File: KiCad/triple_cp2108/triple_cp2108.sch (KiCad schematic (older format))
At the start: 29 parts, among them J1 USB_B, J2 USB_A, J3 Conn_02x20_Odd_Even, U1 MIC5504-3.3YM5, U2 USB2514B_Bi, Y1 24M

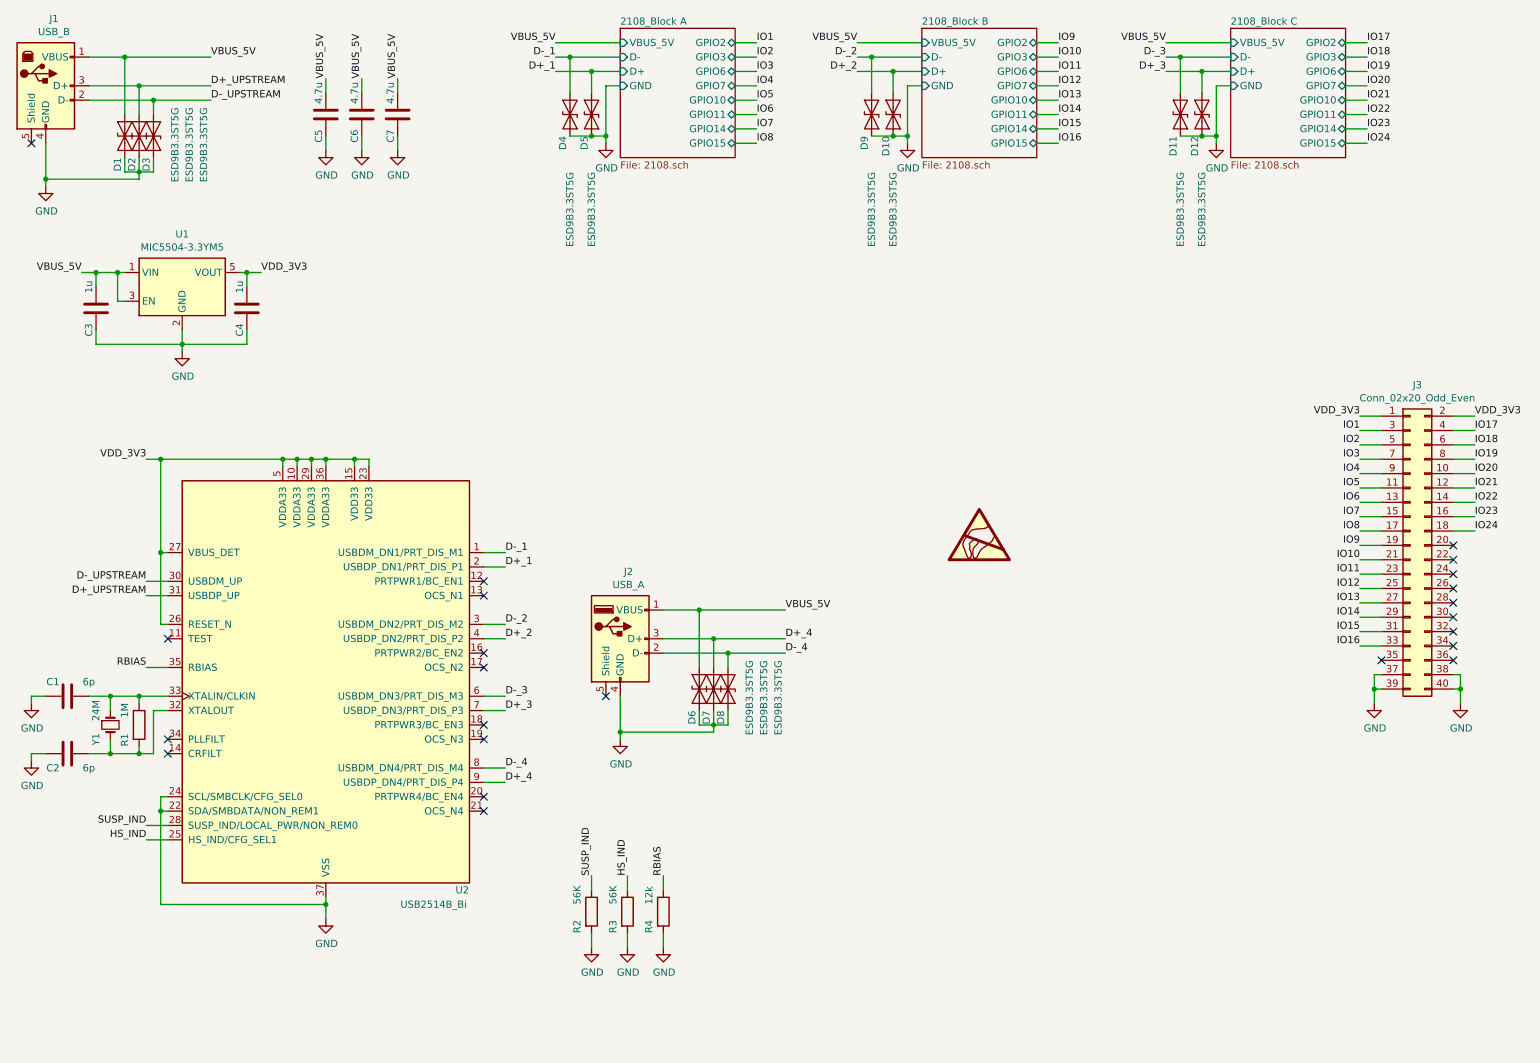
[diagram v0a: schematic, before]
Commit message: 24v added
24v ext pow added
 - in prgs.
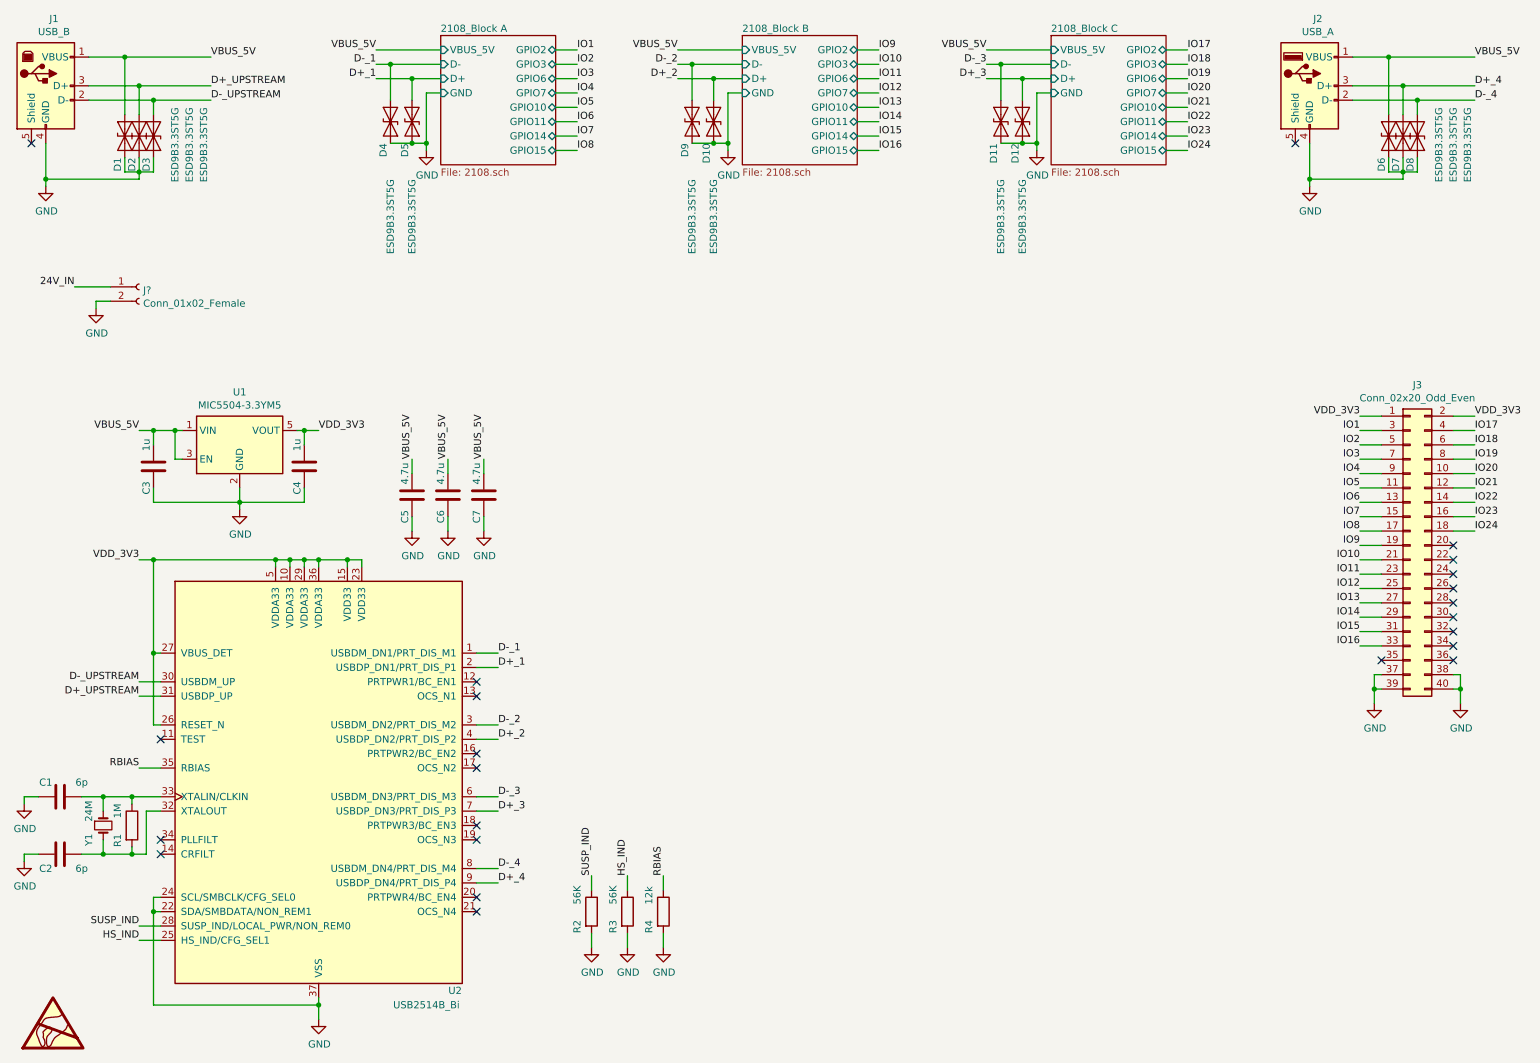
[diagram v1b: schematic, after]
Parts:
- added J?: Conn_01x02_Female, symbol Connector:Conn_01x02_Female
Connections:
- net GND: now also J?.2 (Pin_2)
- new net 24V_IN: J?.1 (Pin_1)
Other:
- moved on the sheet: C1, C2, C3, C4, C5, C6, C7, D10, D11, D12, D4, D5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
